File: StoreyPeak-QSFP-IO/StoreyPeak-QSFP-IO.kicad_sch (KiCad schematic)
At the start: 28 parts, among them U1 QSFP_PCB-QSFP, U3 CH340G, X1 X322512MSB4SI

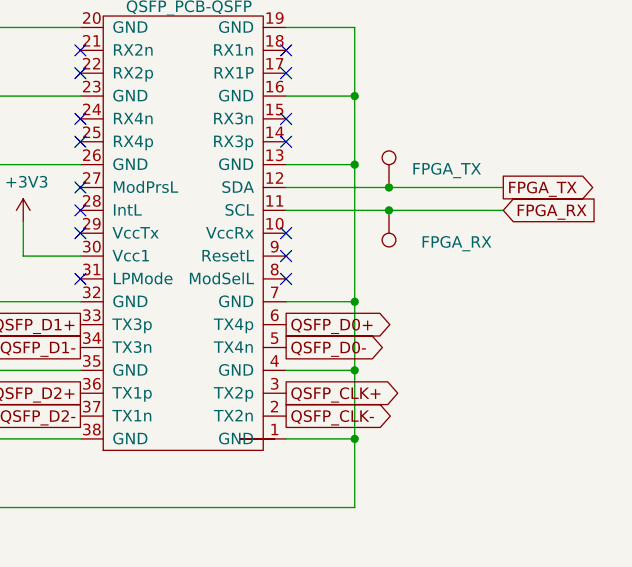
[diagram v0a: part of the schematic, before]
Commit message: Add GND pad next to UART pads, reroute 5V pad to avoid breaking GND plane below HDMI signals
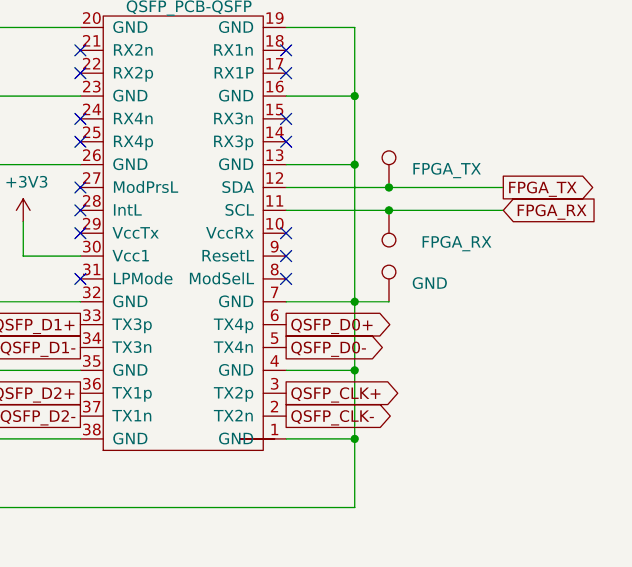
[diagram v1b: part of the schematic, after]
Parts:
- added TP7: GND, TestPoint:TestPoint_Pad_1.5x1.5mm, symbol Connector:TestPoint
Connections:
- net GND: now also TP7.1
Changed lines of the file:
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@@
 	(wire
 		(pts
+			(xy 210.82 133.35) (xy 214.63 133.35)
+		)
+		(stroke
+			(width 0)
+			(type default)
+		)
+	)
+	(wire
+		(pts
 			(xy 16.51 33.02) (xy 39.37 33.02)
 		)
@@
 					(unit 1)
 				)
+			)
+		)
+	)
+	(symbol
+		(lib_id "Connector:TestPoint")
+		(at 214.63 133.35 0)
+		(unit 1)
+		(exclude_from_sim no)
+		(in_bom yes)
+		(on_board yes)
+		(dnp no)
+		(property "Reference" "TP7"
+			(at 217.17 128.7779 0)
+			(effects
+				(font
+					(size 1.27 1.27)
+				)
+				(justify left)
+				(hide yes)
+			)
+		)
+		(property "Value" "GND"
+			(at 217.17 131.3179 0)
+			(effects
+				(font
+					(size 1.27 1.27)
+				)
+				(justify left)
+			)
+		)
+		(property "Footprint" "TestPoint:TestPoint_Pad_1.5x1.5mm"
+			(at 219.71 133.35 0)
+			(effects
+				(font
+					(size 1.27 1.27)
+				)
+				(hide yes)
+			)
+		)
+		(property "Datasheet" "~"
+			(at 219.71 133.35 0)
+			(effects
+				(font
+					(size 1.27 1.27)
+				)
+				(hide yes)
+			)
+		)
+		(property "Description" "test point"
+			(at 214.63 133.35 0)
+			(effects
+				(font
+					(size 1.27 1.27)
+				)
+				(hide yes)
+			)
+		)
+		(pin "1"
+		)
+		(instances
+			(project "StoreyPeak-QSFP-IO"
+				(path "/09a4c8ee-e8d7-4980-8dc1-43a8ae75179d"
+					(reference "TP7")
+					(unit 1)
+				)

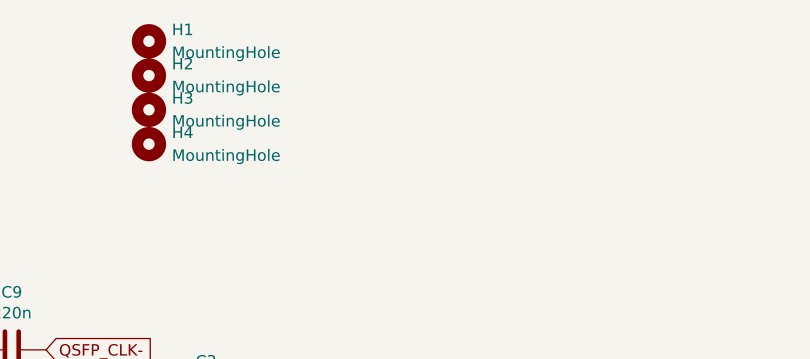
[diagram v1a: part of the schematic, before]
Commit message: Add JLCPCB tooling holes
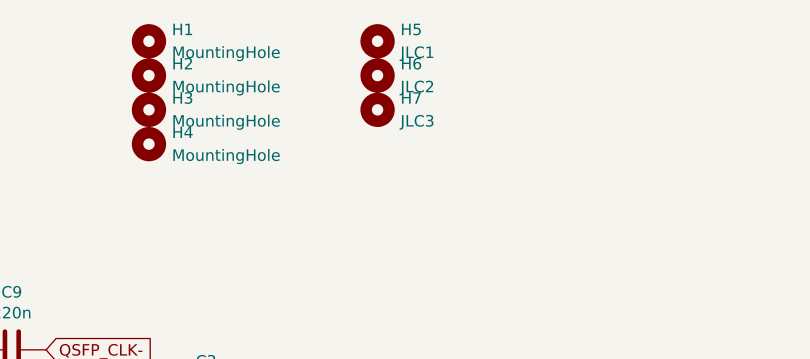
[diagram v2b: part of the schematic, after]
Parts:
- added H5: JLC1, MountingHole:JLCPCB_Tooling_Hole, symbol Mechanical:MountingHole
- added H6: JLC2, MountingHole:JLCPCB_Tooling_Hole, symbol Mechanical:MountingHole
- added H7: JLC3, MountingHole:JLCPCB_Tooling_Hole, symbol Mechanical:MountingHole
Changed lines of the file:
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@@
+	)
+	(symbol
+		(lib_id "Mechanical:MountingHole")
+		(at 132.08 19.05 0)
+		(unit 1)
+		(exclude_from_sim yes)
+		(in_bom no)
+		(on_board yes)
+		(dnp no)
+		(fields_autoplaced yes)
+		(property "Reference" "H5"
+			(at 134.62 17.7799 0)
+			(effects
+				(font
+					(size 1.27 1.27)
+				)
+				(justify left)
+			)
+		)
+		(property "Value" "JLC1"
+			(at 134.62 20.3199 0)
+			(effects
+				(font
+					(size 1.27 1.27)
+				)
+				(justify left)
+			)
+		)
+		(property "Footprint" "MountingHole:JLCPCB_Tooling_Hole"
+			(at 132.08 19.05 0)
+			(effects
+				(font
+					(size 1.27 1.27)
+				)
+				(hide yes)
+			)
+		)
+		(property "Datasheet" "~"
+			(at 132.08 19.05 0)
+			(effects
+				(font
+					(size 1.27 1.27)
+				)
+				(hide yes)
+			)
+		)
+		(property "Description" "Mounting Hole without connection"
+			(at 132.08 19.05 0)
+			(effects
+				(font
+					(size 1.27 1.27)
+				)
+				(hide yes)
+			)
+		)
+		(instances
+			(project ""
+				(path "/09a4c8ee-e8d7-4980-8dc1-43a8ae75179d"
+					(reference "H5")
+					(unit 1)
+				)
+			)
+		)
 	)
 	(symbol
@@
 				(path "/09a4c8ee-e8d7-4980-8dc1-43a8ae75179d"
 					(reference "TP7")
+					(unit 1)
+				)
+			)
+		)
+	)
+	(symbol
+		(lib_id "Mechanical:MountingHole")
+		(at 132.08 22.86 0)
+		(unit 1)
+		(exclude_from_sim yes)
+		(in_bom no)
+		(on_board yes)
+		(dnp no)
+		(fields_autoplaced yes)
+		(property "Reference" "H6"
+			(at 134.62 21.5899 0)
+			(effects
+				(font
+					(size 1.27 1.27)
+				)
+				(justify left)
+			)
+		)
+		(property "Value" "JLC2"
+			(at 134.62 24.1299 0)
+			(effects
+				(font
+					(size 1.27 1.27)
+				)
+				(justify left)
+			)
+		)
+		(property "Footprint" "MountingHole:JLCPCB_Tooling_Hole"
+			(at 132.08 22.86 0)
+			(effects
+				(font
+					(size 1.27 1.27)
+				)
+				(hide yes)
+			)
+		)
+		(property "Datasheet" "~"
+			(at 132.08 22.86 0)
+			(effects
+				(font
+					(size 1.27 1.27)
+				)
+				(hide yes)
+			)
+		)
+		(property "Description" "Mounting Hole without connection"
+			(at 132.08 22.86 0)
+			(effects
+				(font
+					(size 1.27 1.27)
+				)
+				(hide yes)
+			)
+		)
+		(instances
+			(project "StoreyPeak-QSFP-IO"
+				(path "/09a4c8ee-e8d7-4980-8dc1-43a8ae75179d"
+					(reference "H6")
 					(unit 1)
 				)
@@
 					(unit 1)
 				)
+			)
+		)
+	)
+	(symbol
+		(lib_id "Mechanical:MountingHole")
+		(at 132.08 26.67 0)
+		(unit 1)
+		(exclude_from_sim yes)
+		(in_bom no)
+		(on_board yes)
+		(dnp no)
+		(fields_autoplaced yes)
+		(property "Reference" "H7"
+			(at 134.62 25.3999 0)
+			(effects
+				(font
+					(size 1.27 1.27)
+				)
+				(justify left)
+			)
+		)
+		(property "Value" "JLC3"
+			(at 134.62 27.9399 0)
+			(effects
+				(font
+					(size 1.27 1.27)
+				)
+				(justify left)
+			)
+		)
+		(property "Footprint" "MountingHole:JLCPCB_Tooling_Hole"
+			(at 132.08 26.67 0)
+			(effects
+				(font
+					(size 1.27 1.27)
+				)
+				(hide yes)
+			)
+		)
+		(property "Datasheet" "~"
+			(at 132.08 26.67 0)
+			(effects
+				(font
+					(size 1.27 1.27)
+				)
+				(hide yes)
+			)
+		)
+		(property "Description" "Mounting Hole without connection"
+			(at 132.08 26.67 0)
+			(effects
+				(font
+					(size 1.27 1.27)
+				)
+				(hide yes)
+			)
+		)
+		(instances
+			(project "StoreyPeak-QSFP-IO"
+				(path "/09a4c8ee-e8d7-4980-8dc1-43a8ae75179d"
+					(reference "H7")
+					(unit 1)
+				)

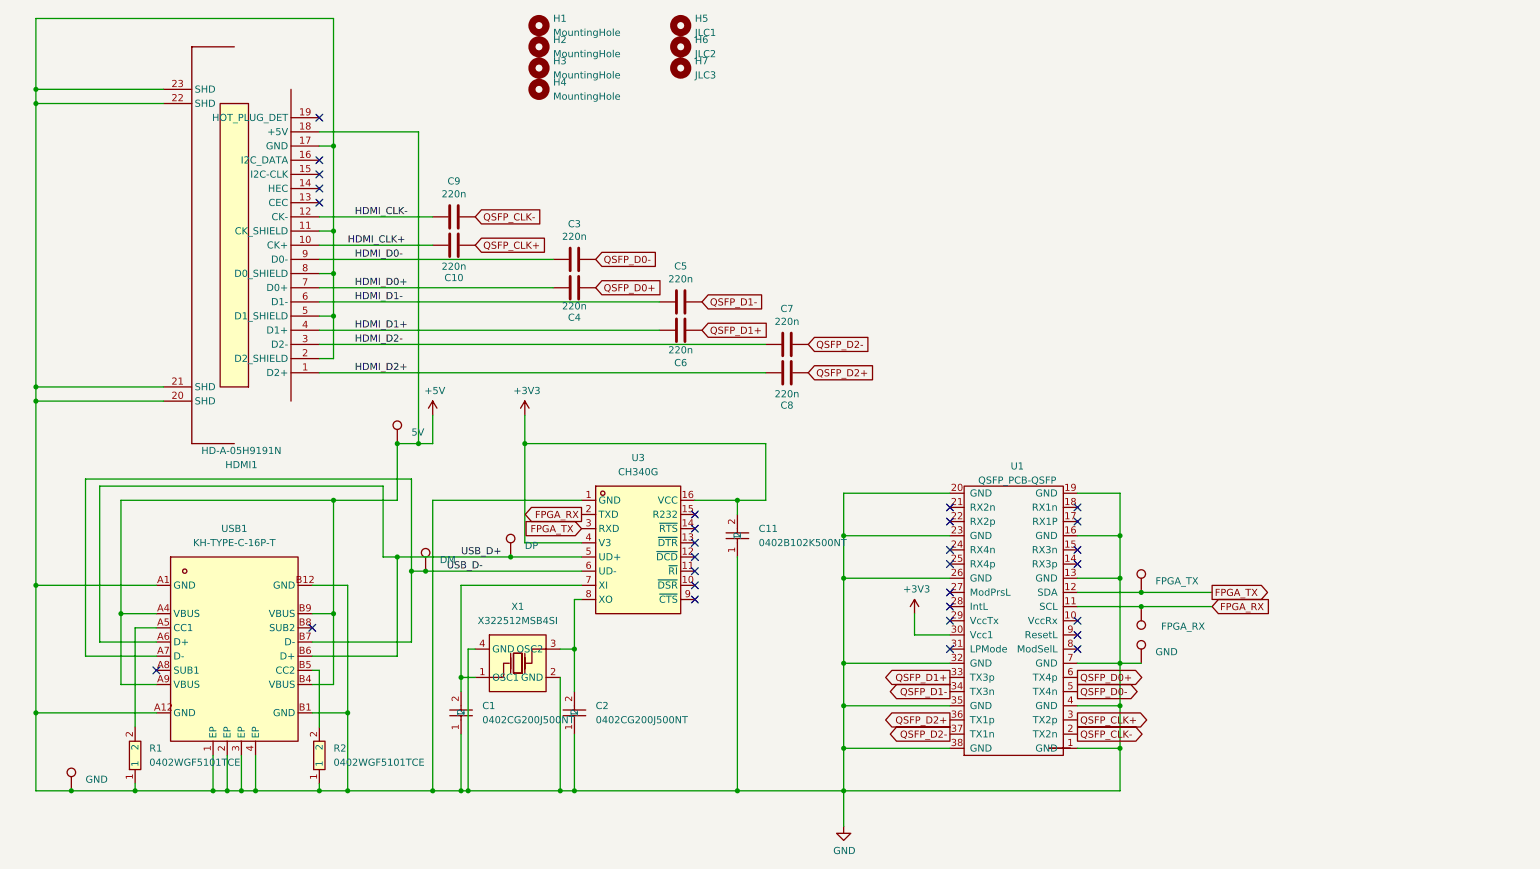
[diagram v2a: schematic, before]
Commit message: Fix board for right QSFP connector, change HDMI caps to 0402
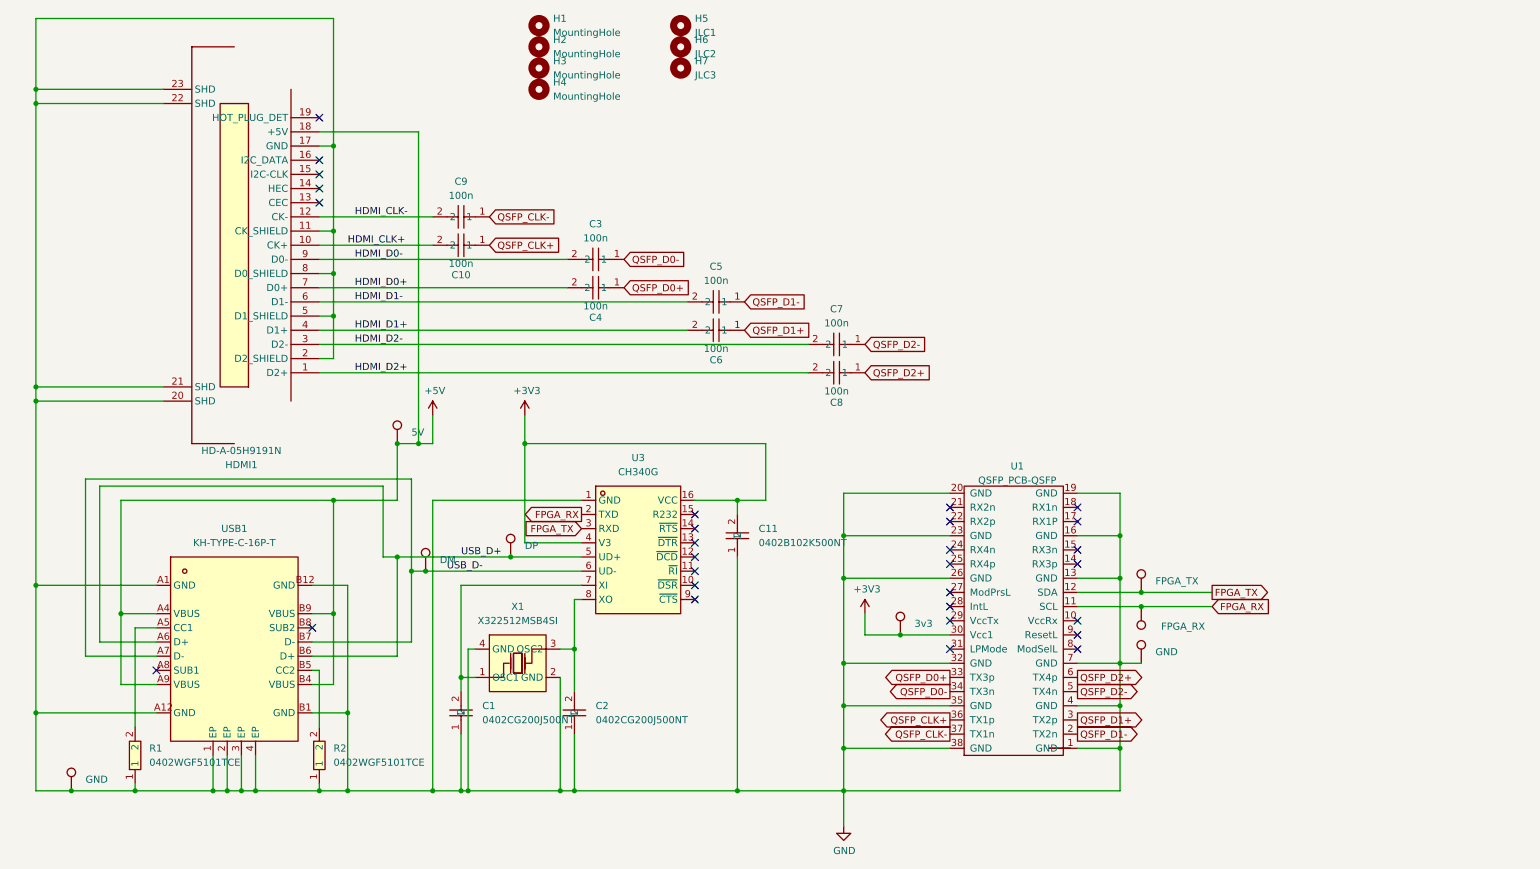
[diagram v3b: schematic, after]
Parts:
- removed C10, C3, C4, C5, C6, C7, C8, C9: 220n, Capacitor_SMD:C_0603_1608Metric_Pad1.08x0.95mm_HandSolder, symbol Device:C
- added C10, C3, C4, C5, C6, C7, C8, C9: 100n, easyeda2kicad:C0402, symbol easyeda2kicad:CL05B104KO5NNNC
- added TP8: 3v3, TestPoint:TestPoint_Pad_1.5x1.5mm, symbol Connector:TestPoint
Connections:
- net +3V3: now also TP8.1
- net HDMI_CLK+: now also C10.2
- net HDMI_CLK-: now also C9.2
- net HDMI_D0+: now also C4.2
- net HDMI_D0-: now also C3.2
- net HDMI_D1+: now also C6.2
- net HDMI_D1-: now also C5.2
- net HDMI_D2+: now also C8.2
- net HDMI_D2-: now also C7.2
- net QSFP_CLK+: now also U1.36 (TX1p), C10.1; no longer U1.3 (TX2p)
- net QSFP_CLK-: now also U1.37 (TX1n), C9.1; no longer U1.2 (TX2n)
- net QSFP_D0+: now also U1.33 (TX3p), C4.1; no longer U1.6 (TX4p)
- net QSFP_D0-: now also U1.34 (TX3n), C3.1; no longer U1.5 (TX4n)
- net QSFP_D1+: now also U1.3 (TX2p), C6.1; no longer U1.33 (TX3p)
- net QSFP_D1-: now also U1.2 (TX2n), C5.1; no longer U1.34 (TX3n)
- net QSFP_D2+: now also U1.6 (TX4p), C8.1; no longer U1.36 (TX1p)
- net QSFP_D2-: now also U1.5 (TX4n), C7.1; no longer U1.37 (TX1n)

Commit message: Get 3.3V from LDO off USB port
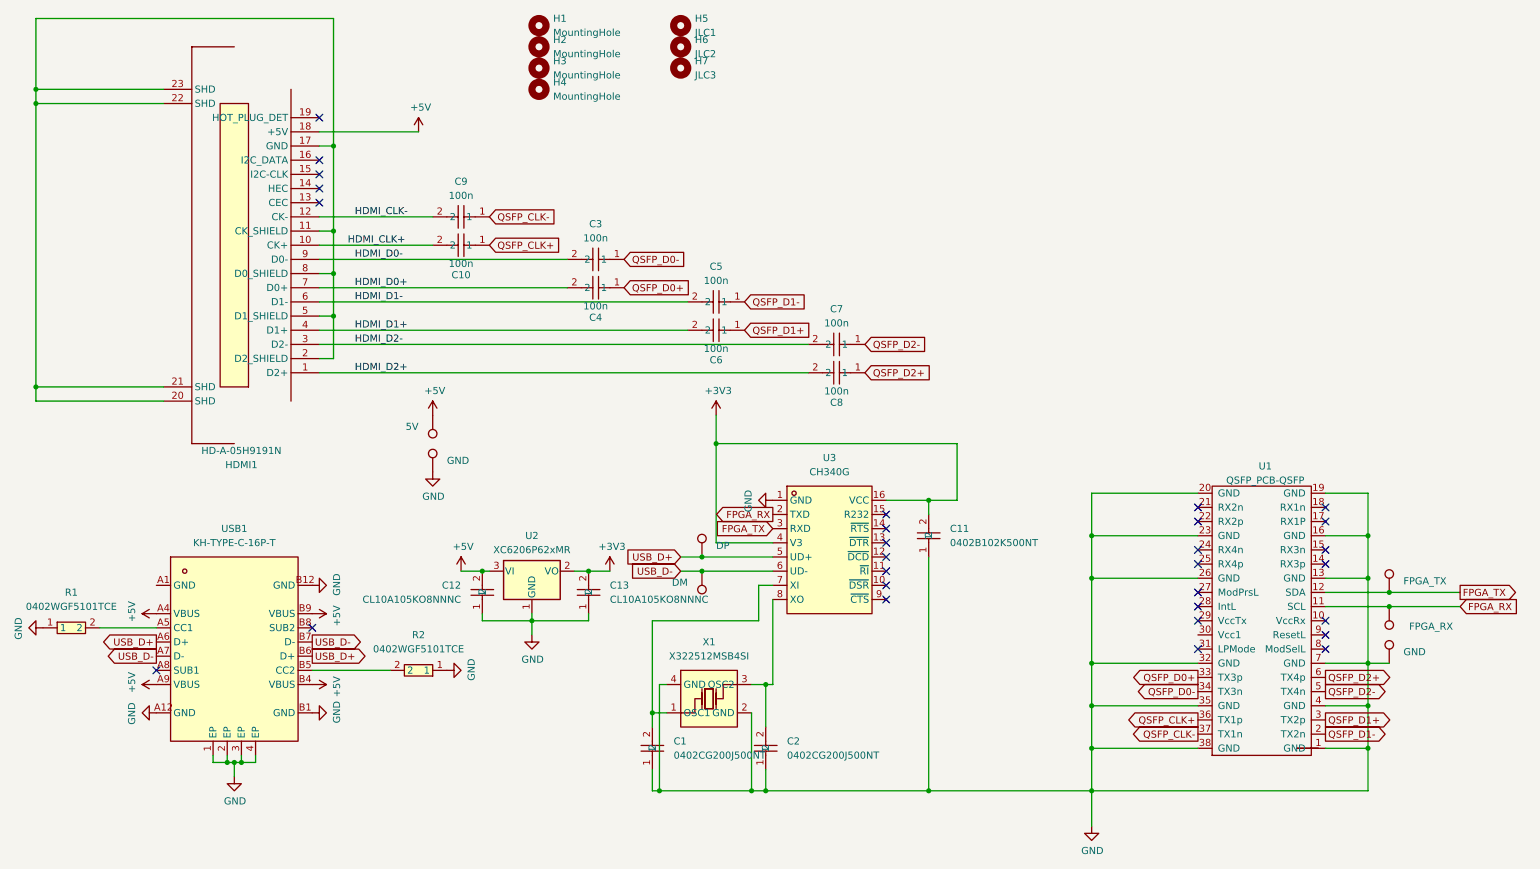
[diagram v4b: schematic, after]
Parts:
- removed TP8: 3v3, TestPoint:TestPoint_Pad_1.5x1.5mm, symbol Connector:TestPoint
- added C12, C13: CL10A105KO8NNNC, Capacitor_SMD:C_0603_1608Metric, symbol LCSC:CL10A105KO8NNNC
- added U2: XC6206P62xMR, Package_TO_SOT_SMD:SOT-23-3, symbol Regulator_Linear:XC6206PxxxMR
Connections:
- net +3V3: now also C13.2, U2.2 (VO); no longer U1.30 (Vcc1)
- net +5V: now also C12.2, U2.3 (VI)
- net GND: now also C12.1, C13.1, U2.1 (GND); no longer HDMI1.11 (CK_SHIELD), HDMI1.17 (GND), HDMI1.2 (D2_SHIELD), HDMI1.20 (SHD), HDMI1.21 (SHD), HDMI1.22 (SHD), HDMI1.23 (SHD), HDMI1.5 (D1_SHIELD), HDMI1.8 (D0_SHIELD), USB1.A1 (GND)
- new net: HDMI1.11 (CK_SHIELD), HDMI1.17 (GND), HDMI1.2 (D2_SHIELD), HDMI1.20 (SHD), HDMI1.21 (SHD), HDMI1.22 (SHD), HDMI1.23 (SHD), HDMI1.5 (D1_SHIELD), HDMI1.8 (D0_SHIELD)
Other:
- moved on the sheet: C1, C11, C2, R1, R2, U1, U3, X1

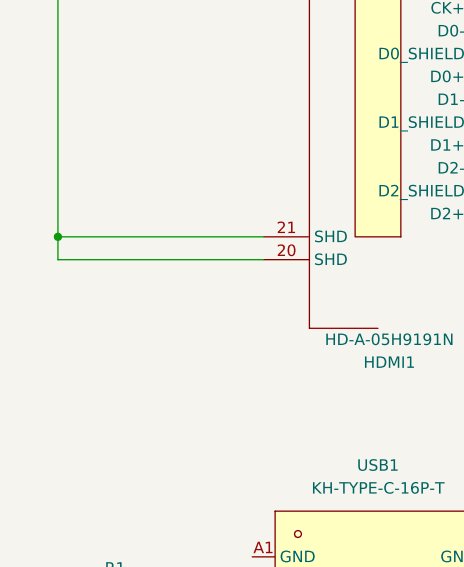
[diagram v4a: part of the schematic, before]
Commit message: Connect HDMI ground pins
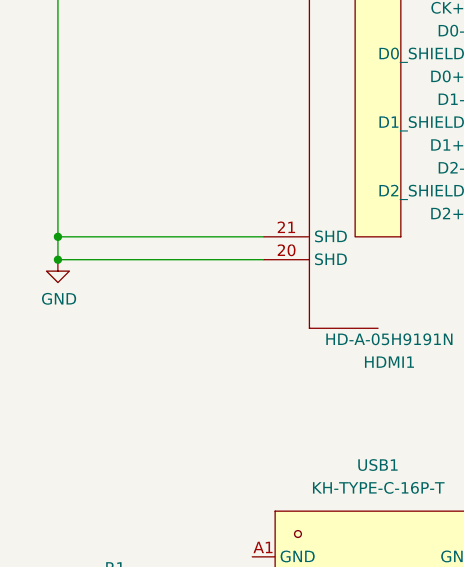
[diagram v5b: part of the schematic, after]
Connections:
- net GND: now also HDMI1.11 (CK_SHIELD), HDMI1.17 (GND), HDMI1.2 (D2_SHIELD), HDMI1.20 (SHD), HDMI1.21 (SHD), HDMI1.22 (SHD), HDMI1.23 (SHD), HDMI1.5 (D1_SHIELD), HDMI1.8 (D0_SHIELD)
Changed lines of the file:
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@@
 	)
 	(junction
+		(at 16.51 86.36)
+		(diameter 0)
+		(color 0 0 0 0)
+	)
+	(junction
 		(at 205.74 118.11)
 		(diameter 0)
@@
 					(unit 1)
 				)
+			)
+		)
+	)
+	(symbol
+		(lib_id "power:GND")
+		(at 16.51 86.36 0)
+		(unit 1)
+		(exclude_from_sim no)
+		(in_bom yes)
+		(on_board yes)
+		(dnp no)
+		(property "Reference" "#PWR015"
+			(at 16.51 92.71 0)
+			(effects
+				(font
+					(size 1.27 1.27)
+				)
+				(hide yes)
+			)
+		)
+		(property "Value" "GND"
+			(at 16.637 90.7542 0)
+			(effects
+				(font
+					(size 1.27 1.27)
+				)
+			)
+		)
+		(property "Footprint" ""
+			(at 16.51 86.36 0)
+			(effects
+				(font
+					(size 1.27 1.27)
+				)
+				(hide yes)
+			)
+		)
+		(property "Datasheet" ""
+			(at 16.51 86.36 0)
+			(effects
+				(font
+					(size 1.27 1.27)
+				)
+				(hide yes)
+			)
+		)
+		(property "Description" ""
+			(at 16.51 86.36 0)
+			(effects
+				(font
+					(size 1.27 1.27)
+				)
+				(hide yes)
+			)
+		)
+		(pin "1"
+		)
+		(instances
+			(project "StoreyPeak-QSFP-IO"
+				(path "/09a4c8ee-e8d7-4980-8dc1-43a8ae75179d"
+					(reference "#PWR015")
+					(unit 1)
+				)

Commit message: Fix wrong footprint for QSFP edge connector
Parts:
- U1: footprint CarlosEDP_Lib:QSFP_PCB -> natanbc:QSFP-Edge
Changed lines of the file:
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@@
 			)
 		)
-		(property "Footprint" "CarlosEDP_Lib:QSFP_PCB"
+		(property "Footprint" "natanbc:QSFP-Edge"
 			(at 234.95 99.06 0)
 			(effects
